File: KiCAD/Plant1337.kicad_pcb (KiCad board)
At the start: 4 copper layers, 59.1 x 41.9 mm, 58 parts, among them J1 USB_B_Micro, J2 Edge2x6_Connector, Q1 AO3400A, Q2 AO3400A, Q3 AO3400A, Q4 AO3400A, U1 SHTC3, U2 ESP32-WROOM-32, U3 AMS1117-3.3

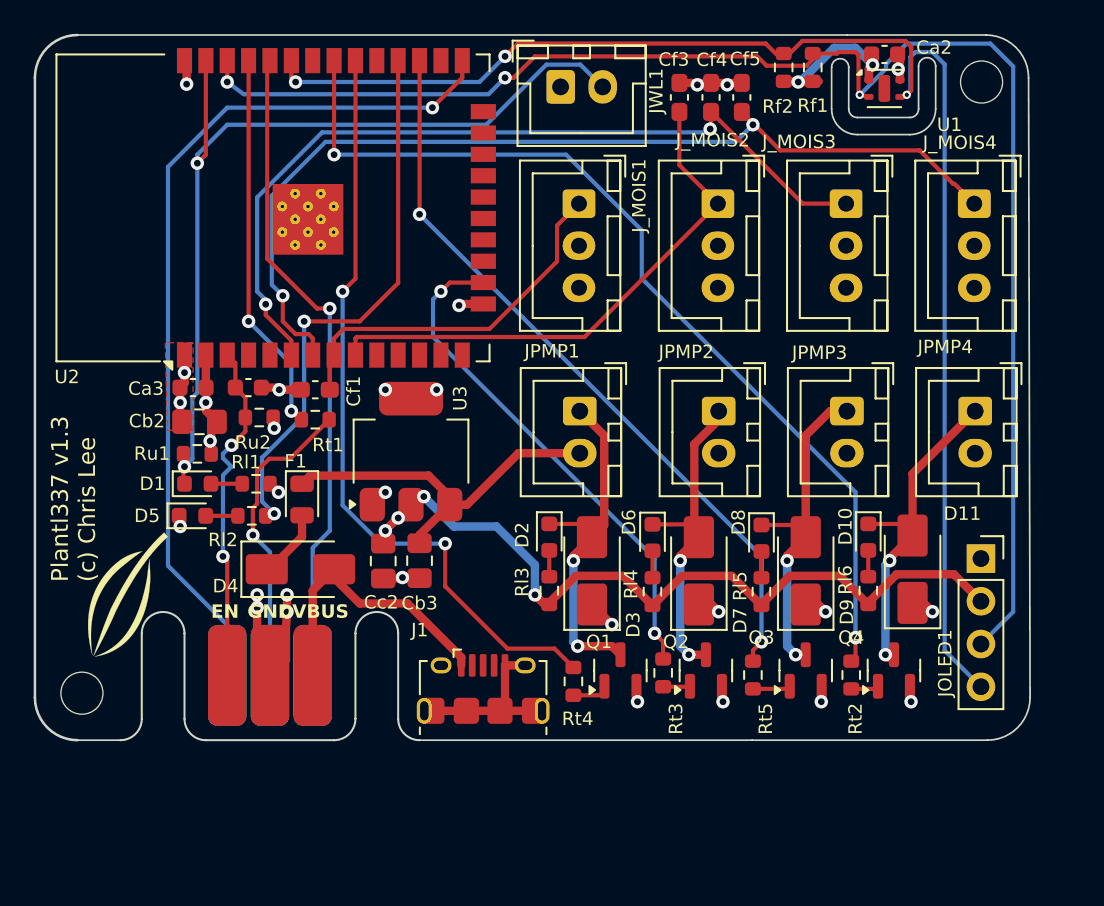
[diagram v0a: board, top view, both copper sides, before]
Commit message: Version 1.0.0 (#42)
### Added
- **Hardware Board v2.x & ESP32-S3 Support**: Added PlatformIO configurations (`esp32s3`, `usb_s3`, `wifi_s3`), `BOARD_V20` pin mappings for `ESP32-S3-WROOM-1-N8R2` with USB-C, updated KiCAD schematics/PCB layouts (v2.0–v2.2 with boot/reset push-buttons and improved flyback diode placement), and BOM (`KiCAD/Plant133.csv`).
- **3D-Printed Enclosure & Accessories**:
  - Updated EBox (`scad/box/`) for Board v2.1+ and added OLED support bracket (`OLEDSupport.scad`) and board test fixture (`fixture.scad`).
  - Added reservoir cover/cap (`scad/reservoir_cover/`) with cutouts for the EBox, tubing, and wires.
  - Updated reservoir insert (`scad/reservoir_insert/`) and extracted reusable vitamin models (`vertical_pump.scad`, `float.scad`).
  - Updated solder stencil fixture and added stencil edge-support frame (`scad/stencil_fixture/`).
- **Adafruit IO & SSL/TLS MQTT Support**: Added NTP time synchronization (`og3::Ntp`), SSL/TLS with optional certificate verification, and Adafruit IO MQTT mode with feed filtering/rate-limiting in both firmware and the Svelte MQTT configuration UI.
- **System Status Versioning**: Exposed `software` and `hardware` version fields in `GET /api/status`.
- **Native Unit Tests & Dependabot**: Ported unit tests (`test/test_watering/test_watering.cpp`) to `og3` under `[env:native]`, enabled `pio test -e native` in `util/check.sh`, and added GitHub Actions Dependabot configuration.

### Changed
- **Framework Upgrade**: Upgraded to **og3 v0.7.0**, **og3x-oled v0.6.1**, and **og3x-shtc3 v0.6.0**, linking modules by pointer via `require(...)` and making `DoseLog` an `og3::Module`.
- **Web UI & API Alignment**: Updated Svelte WiFi and MQTT configuration pages to use `og3` variable keys (`essId`, `wifiPassword`, `hostAddr`, `authUser`, `authPassword`) and updated `build-svelte.sh` to use `--etag=always`.
- **MQTT Optimization**: Avoided sending duplicate reservoir status updates per plant.

### Fixed
- **Plant API Validation*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
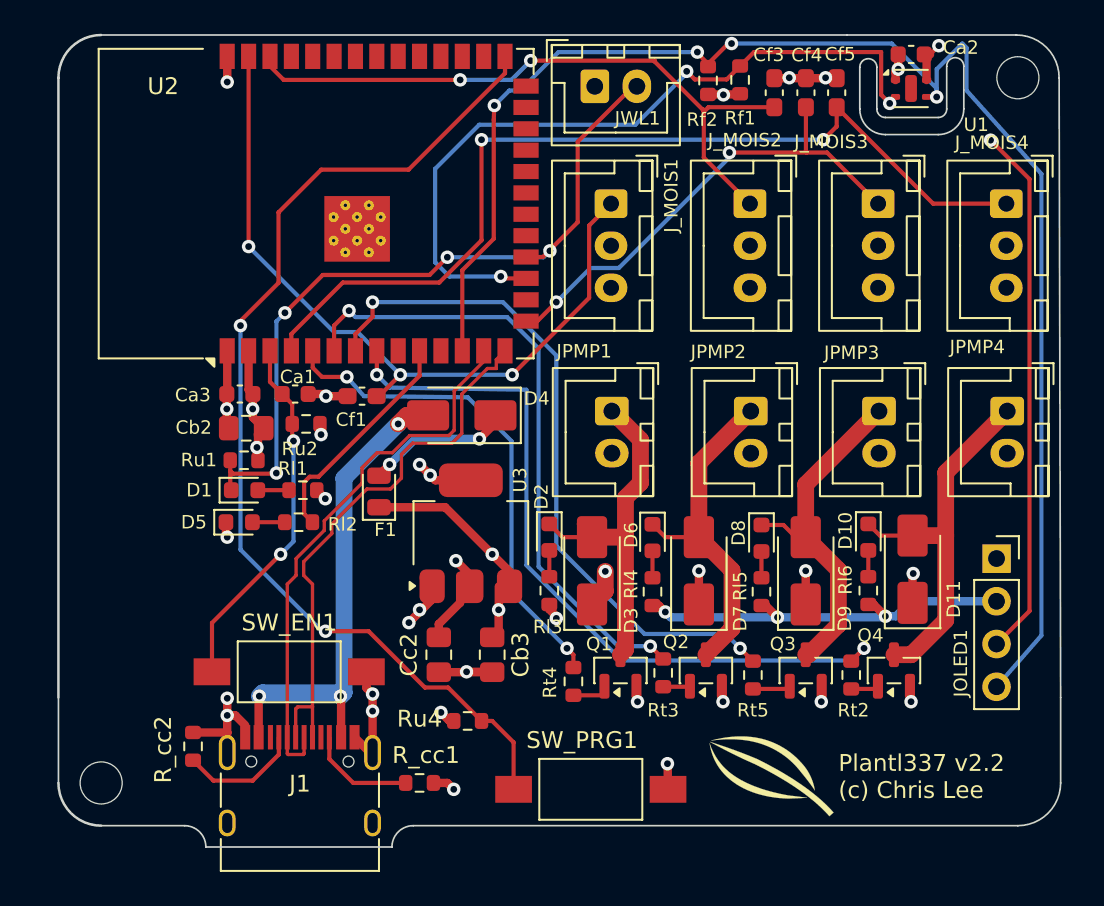
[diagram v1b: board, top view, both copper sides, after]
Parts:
- removed J2: Edge2x6_Connector, Library:EdgeConnector_2x3
- removed Rt1: 470, Resistor_SMD:R_0603_1608Metric
- added R_cc1: 5.1k, Resistor_SMD:R_0603_1608Metric, F.Cu at (69.8, 104.1)
- added R_cc2: 5.1k, Resistor_SMD:R_0603_1608Metric, F.Cu at (56.4, 102.0)
- added Ru4: 10k, Resistor_SMD:R_0603_1608Metric, F.Cu at (72.7, 100.5)
- added SW_EN1: SW_Push, Button_Switch_SMD:SW_SPST_FSMSM, F.Cu at (62.1, 97.5)
- added SW_PRG1: SW_Push, Button_Switch_SMD:SW_SPST_FSMSM, F.Cu at (80.0, 104.5)
- J1: value USB_B_Micro -> USB_C_Receptacle_USB2.0_16P; footprint Connector_USB:USB_Micro-B_Amphenol_10118194_Horizontal -> Connector_USB:USB_C_Receptacle_HRO_TYPE-C-31-M-12
- U2: value ESP32-WROOM-32 -> ESP32-S3-WROOM-1; footprint RF_Module:ESP32-WROOM-32 -> RF_Module:ESP32-S3-WROOM-1
- moved D4 13.2 mm to (72.4, 82.3), turned to 180 degrees
- moved J1 12.9 mm to (62.7, 105.5)
- moved Cb3 7.06 mm to (74.2, 96.5)
- moved Cc2 6.47 mm to (71.0, 96.5)
- moved U3 6.01 mm to (72.9, 89.3)
- moved Cf3 5.65 mm to (90.9, 63.1)
- moved Cf4 5.65 mm to (92.8, 63.1)
- moved Cf5 5.65 mm to (94.6, 63.1)
- moved REF** 5.46 mm to (50.9, 104.1)
- moved F1 4.60 mm to (67.4, 86.8), turned to 90 degrees
- moved Rf2 4.56 mm to (87.0, 62.4)
- moved Rf1 4.38 mm to (88.9, 62.4)
- moved D1 2.81 mm to (59.4, 86.7)
- moved Ca1 2.81 mm to (62.5, 81.0)
- moved Ca3 2.81 mm to (59.2, 81.0)
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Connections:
- net EN renamed Net-(U2-EN)
- U2 pad 10: unconnected-(U2-IO25-Pad10) -> GPIO17
- U2 pad 12: unconnected-(U2-IO27-Pad12) -> SDA1
- U2 pad 13: unconnected-(U2-IO14-Pad13) -> USB_D-
- U2 pad 14: unconnected-(U2-IO12-Pad14) -> USB_D+
- U2 pad 15: GND -> ADC1_CH6
- U2 pad 16: P2 -> unconnected-(U2-IO46-Pad16)
- U2 pad 17: unconnected-(U2-SHD/SD2-Pad17) -> SCL1
- U2 pad 18: unconnected-(U2-SWP/SD3-Pad18) -> WL
- U2 pad 25: GPIO0 -> unconnected-(U2-IO48-Pad25)
- U2 pad 27: P3 -> Net-(U2-IO0)
- U2 pad 28: GPIO17 -> unconnected-(U2-IO35-Pad28)
- U2 pad 30: P1 -> unconnected-(U2-IO37-Pad30)
- U2 pad 31: P4 -> unconnected-(U2-IO38-Pad31)
- U2 pad 33: SDA1 -> unconnected-(U2-IO40-Pad33)
- U2 pad 34: TXC -> unconnected-(U2-IO41-Pad34)
- U2 pad 35: TX -> unconnected-(U2-IO42-Pad35)
- U2 pad 36: SCL1 -> unconnected-(U2-RXD0-Pad36)
- U2 pad 37: WL -> unconnected-(U2-TXD0-Pad37)
- U2 pad 38: GND -> ADC1_CH5
- U2 pad 39: GND -> ADC1_CH4
- U2 pad 4: unconnected-(U2-SENSOR_VP-Pad4) -> ADC1_CH7
- U2 pad 5: unconnected-(U2-SENSOR_VN-Pad5) -> P1
- U2 pad 6: ADC1_CH6 -> P2
- U2 pad 7: ADC1_CH7 -> P3
- U2 pad 8: ADC1_CH4 -> P4
- U2 pad 9: ADC1_CH5 -> unconnected-(U2-IO16-Pad9)
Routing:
- net Net-(U2-IO0): track 0.00 -> 62.7 mm, vias 0 -> 2
- net GPIO0: track 52.4 -> 0.00 mm, vias 1 -> 0
- net TXC: track 39.0 -> 0.00 mm, vias 1 -> 0
- net USB_D-: track 0.00 -> 33.0 mm
- net USB_D+: track 0.00 -> 32.0 mm
- net TX: track 22.7 -> 0.00 mm, vias 2 -> 0
- net ADC1_CH4: track 22.3 -> 44.7 mm, vias 0 -> 3
- net ADC1_CH6: track 50.1 -> 29.2 mm
- net GPIO17: track 33.1 -> 13.5 mm, vias 2 -> 0
- net RXC: track 18.2 -> 0.00 mm, vias 1 -> 0
- net P1: track 45.9 -> 29.6 mm
- net +3.3V: track 84.5 -> 97.9 mm, vias 12 -> 14
- net P4: track 56.7 -> 44.8 mm
- net VBUS: track 17.3 -> 28.5 mm, vias 0 -> 3
- net WL: track 53.9 -> 45.2 mm, vias 2 -> 4
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- removed copper zone on F.Cu, net GND
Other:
- board size 59.1 x 41.9 mm -> 59.6 x 48.3 mm
- board text added: "Plantl337 v2.2 (c) Chris Lee"
- board text removed: "EN"
- board text removed: "GND"
- board text removed: "IO0"
- board text removed: "Plantl337 v1.3 (c) Chris Lee"
- board text removed: "RX"
- board text removed: "TX"
- board text removed: "VBUS"
